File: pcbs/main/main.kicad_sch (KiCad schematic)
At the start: 17 parts, among them J1 JST_XH_B3B, J3 JST_XH_B3B, J4 XT30PW-M, U1 ESP32-DEVKITC-32U, U2 74HC595, U3 74HC595

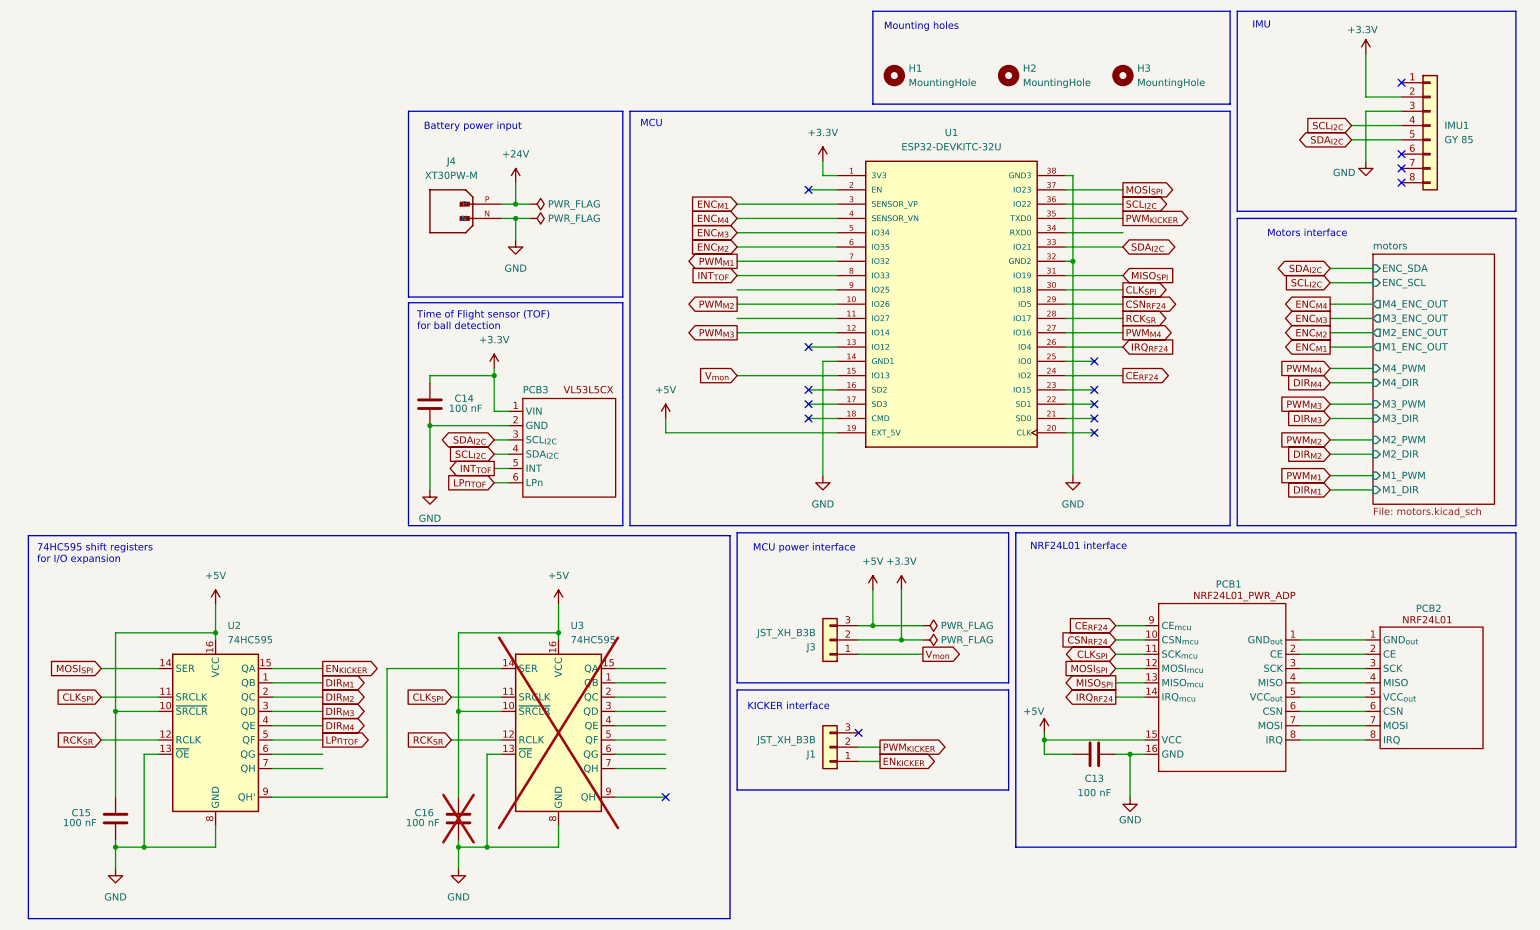
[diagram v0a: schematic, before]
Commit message: Add circuit for motor feedback
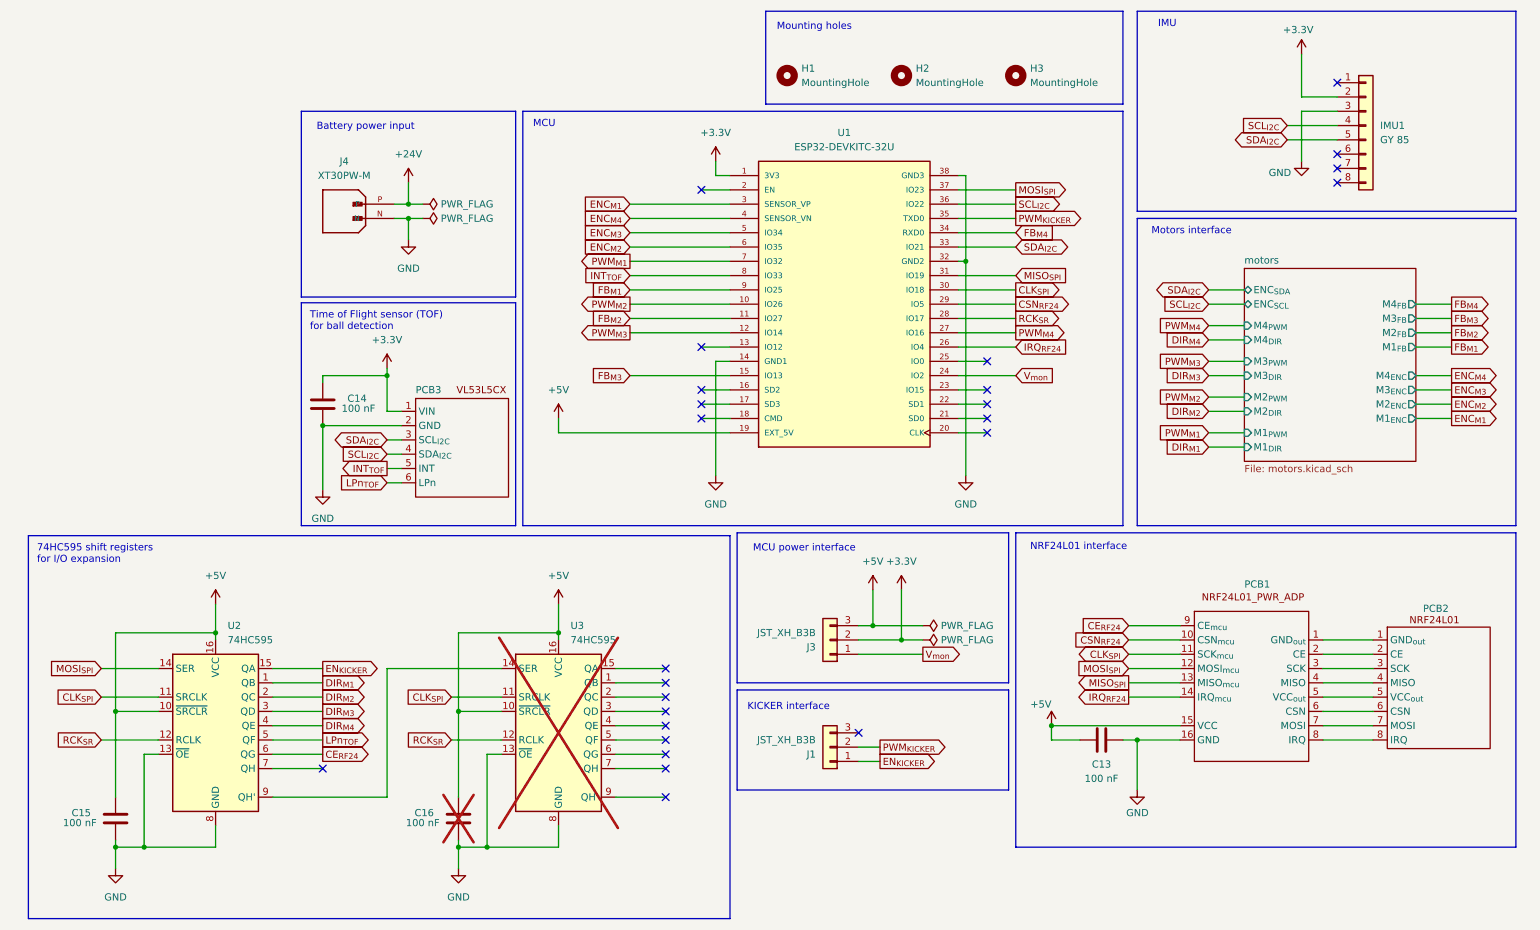
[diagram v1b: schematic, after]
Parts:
- J4: symbol XT30PW-M:XT30PW-M -> oxebots:XT30PW-M
- U1: symbol ESP32-DEVKITC-32U:ESP32-DEVKITC-32U -> oxebots:ESP32-DEVKITC-32U
- U2: footprint (none) -> Package_DIP:DIP-16_W7.62mm
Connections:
- net CE_{RF24}: now also U2.6 (QG); no longer U1.24 (IO2)
- net V_{mon}: now also U1.24 (IO2); no longer U1.15 (IO13)
- net FB_{M2}: now reaches U1.11 (IO27)
- net FB_{M4}: now reaches U1.34 (RXD0)
- net FB_{M1}: now reaches U1.9 (IO25)
- new net FB_{M3}: U1.15 (IO13)
- no-connect marks 16 -> 25
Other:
- sheet motors ports: added ENC_{SCL}, ENC_{SDA}, M1_{DIR}, M1_{ENC}, M1_{FB}, M1_{PWM}, M2_{DIR}, M2_{ENC}, M2_{FB}, M2_{PWM}, M3_{DIR}, M3_{ENC}, M3_{FB}, M3_{PWM}, M4_{DIR}, M4_{ENC}, M4_{FB}, M4_{PWM}; removed ENC_SCL, ENC_SDA, M1_DIR, M1_ENC_OUT, M1_PWM, M2_DIR, M2_ENC_OUT, M2_PWM, M3_DIR, M3_ENC_OUT, M3_PWM, M4_DIR, M4_ENC_OUT, M4_PWM
- moved on the sheet: C13, C14, H1, H2, H3, IMU1, J4, PCB1, PCB2, PCB3, U1

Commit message: Add some probes & update footprints
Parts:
- added TP1, TP2, TP3, TP7, TP8: TestPoint_Probe, TestPoint:TestPoint_Loop_D2.50mm_Drill1.0mm_LowProfile, symbol Connector:TestPoint_Probe
- added TP4, TP5, TP6: TestPoint_Probe, TestPoint:TestPoint_Pad_D1.0mm, symbol Connector:TestPoint_Probe
- C1: renamed from C15; footprint Capacitor_THT:C_Disc_D5.0mm_W2.5mm_P2.50mm -> Capacitor_SMD:C_0603_1608Metric
- C2: renamed from C14; footprint Capacitor_THT:C_Disc_D5.0mm_W2.5mm_P2.50mm -> Capacitor_SMD:C_0603_1608Metric
- C4: renamed from C13; footprint Capacitor_THT:C_Disc_D5.0mm_W2.5mm_P2.50mm -> Capacitor_SMD:C_0603_1608Metric
- renumbered C16 to C3, J4 to J1, J3 to J2, J1 to J3, PCB3 to PCB1, PCB1 to PCB2, PCB2 to PCB3, U2 to U1, U3 to U2, U1 to U3
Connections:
- net +24V: now also TP5.1
- net +3.3V: now also TP4.1, TP7.1, TP8.1
- net +5V: now also TP6.1
- net CLK_{SPI}: now also TP1.1
- net MOSI_{SPI}: now also TP2.1
- net RCK_{SR}: now also TP3.1
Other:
- moved on the sheet: J2
